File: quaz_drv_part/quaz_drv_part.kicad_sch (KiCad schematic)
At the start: 47 parts, among them J1 TX, J2 sound, J3 curs, J4 tx_src, J5 phones, J6 PWR, J7 speaker, J8 5Vout, J9 5Vout, U1 MC34119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

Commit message: add some settings
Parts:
- C22: value 1.0 -> 22
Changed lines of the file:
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@@
       (effects (font (size 1.27 1.27)) (justify right))
     )
-    (property "Value" "1.0" (id 1) (at 78.74 88.8999 0)
+    (property "Value" "22" (id 1) (at 78.74 88.8999 0)
       (effects (font (size 1.27 1.27)) (justify right))
     )
@@
     )
     (path "/cc4d460c-9ceb-4879-870b-15d27f563e3c"
-      (reference "C22") (unit 1) (value "1.0") (footprint "Capacitor_SMD:C_1206_3216Metric_Pad1.33x1.80mm_HandSolder")
+      (reference "C22") (unit 1) (value "22") (footprint "Capacitor_SMD:C_1206_3216Metric_Pad1.33x1.80mm_HandSolder")
     )
     (path "/27468505-7382-4386-9f44-4b3f39b41a90"

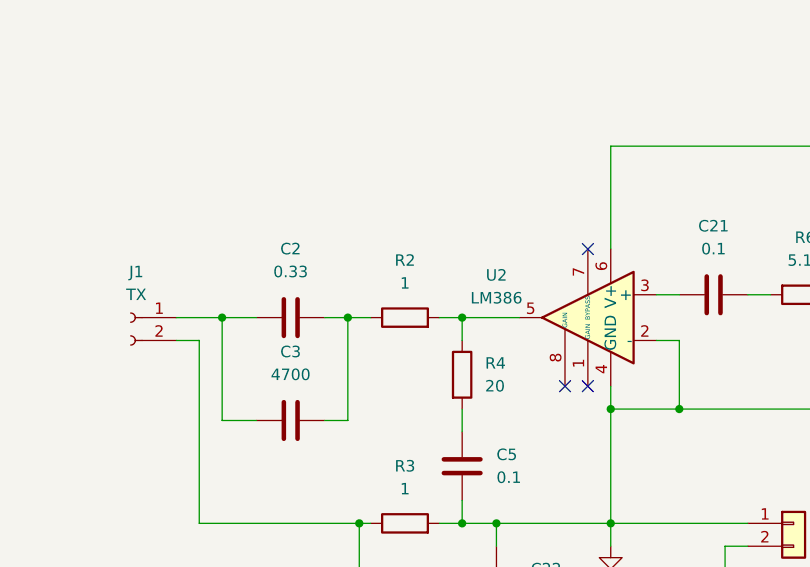
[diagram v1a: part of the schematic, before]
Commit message: ILI9341 -> ST7789
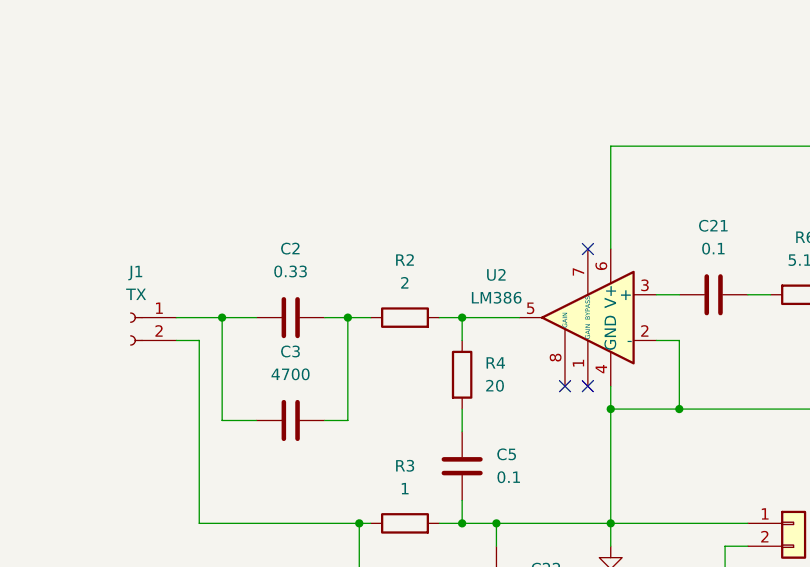
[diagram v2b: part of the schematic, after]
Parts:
- R2: value 1 -> 2
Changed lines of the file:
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@@
     (in_bom yes) (on_board yes) (fields_autoplaced)
     (property "Reference" "R2" (id 0) (at 64.77 52.07 90))
-    (property "Value" "1" (id 1) (at 64.77 54.61 90))
+    (property "Value" "2" (id 1) (at 64.77 54.61 90))
     (property "Footprint" "Resistor_THT:R_Axial_Power_L20.0mm_W6.4mm_P7.62mm_Vertical" (id 2) (at 64.77 60.198 90)
       (effects (font (size 1.27 1.27)) hide)
@@
     )
     (path "/1ccf423b-e242-4647-88be-a60f0c1527b0"
-      (reference "R2") (unit 1) (value "1") (footprint "Resistor_THT:R_Axial_Power_L20.0mm_W6.4mm_P7.62mm_Vertical")
+      (reference "R2") (unit 1) (value "2") (footprint "Resistor_THT:R_Axial_Power_L20.0mm_W6.4mm_P7.62mm_Vertical")
     )
     (path "/1838c54b-71ef-4c33-815a-8f395d759ee0"
